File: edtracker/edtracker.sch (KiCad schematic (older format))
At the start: 3 parts, among them SW1 SW_Push_Dual

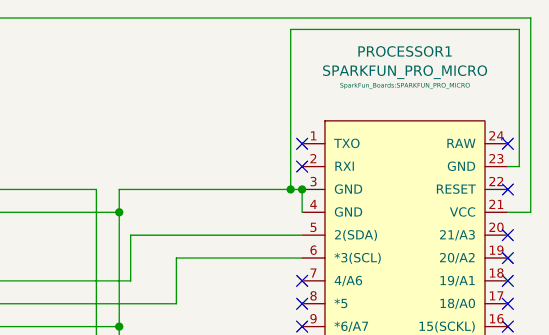
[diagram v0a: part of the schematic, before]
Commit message: changed processor -> microprocessor updated silkscreen
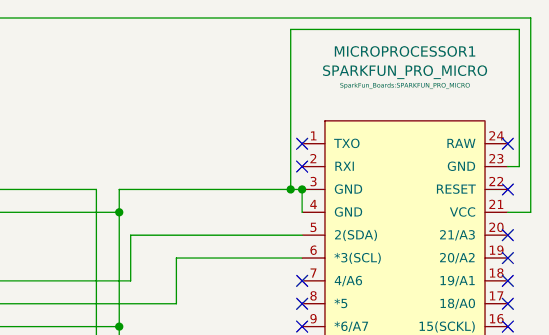
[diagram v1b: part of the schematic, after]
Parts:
- renumbered PROCESSOR1 to MICROPROCESSOR1
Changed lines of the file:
@@
 $EndComp
 $Comp
-L SparkFun-Boards:SPARKFUN_PRO_MICRO PROCESSOR1
+L SparkFun-Boards:SPARKFUN_PRO_MICRO MICROPROCESSOR1
 U 1 1 5FF23269
 P 5000 2700
-F 0 "PROCESSOR1" H 5000 3652 45  0000 C CNN
+F 0 "MICROPROCESSOR1" H 5000 3652 45  0000 C CNN
 F 1 "SPARKFUN_PRO_MICRO" H 5000 3568 45  0000 C CNN
 F 2 "SparkFun_Boards:SPARKFUN_PRO_MICRO" H 5000 3505 20  0000 C CNN

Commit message: added 5v power port
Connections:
- net +5V: now reaches MICROPROCESSOR1.21 (VCC), SENSOR1.1 (VCC)
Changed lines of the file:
@@
 	3100 3050 3100 1600
-Wire Wire Line
-	3100 1600 5550 1600
 Wire Wire Line
 	5550 1600 5550 2450
@@
 	3000 2850 4000 2850
 NoConn ~ 3000 2150
+Wire Wire Line
+	3650 1600 5550 1600
+Wire Wire Line
+	3100 1600 3650 1600
+Connection ~ 3650 1600
+$Comp
+L power:+5V #PWR0102
+U 1 1 600BA7A0
+P 3650 1600
+F 0 "#PWR0102" H 3650 1450 50  0001 C CNN
+F 1 "+5V" H 3665 1773 50  0000 C CNN
+F 2 "" H 3650 1600 50  0001 C CNN
+F 3 "" H 3650 1600 50  0001 C CNN
+	1    3650 1600
+	1    0    0    -1
+$EndComp
 $EndSCHEMATC

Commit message: connected fsync to ground according to mpu spec
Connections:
- net GND: now also SENSOR1.10 (FSYNC)
- no-connect marks 20 -> 19
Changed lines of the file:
@@
 Wire Wire Line
 	3000 2850 4000 2850
-NoConn ~ 3000 2150
 Wire Wire Line
 	3650 1600 5550 1600
@@
 	1    0    0    -1
 $EndComp
+Wire Wire Line
+	3000 2150 3750 2150
+Wire Wire Line
+	3750 2150 3750 2350
+Connection ~ 3750 2350
 $EndSCHEMATC
